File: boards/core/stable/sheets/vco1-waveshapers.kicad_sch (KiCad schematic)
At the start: 41 parts, among them U210 TL072, U211 TL072, U6 TL072

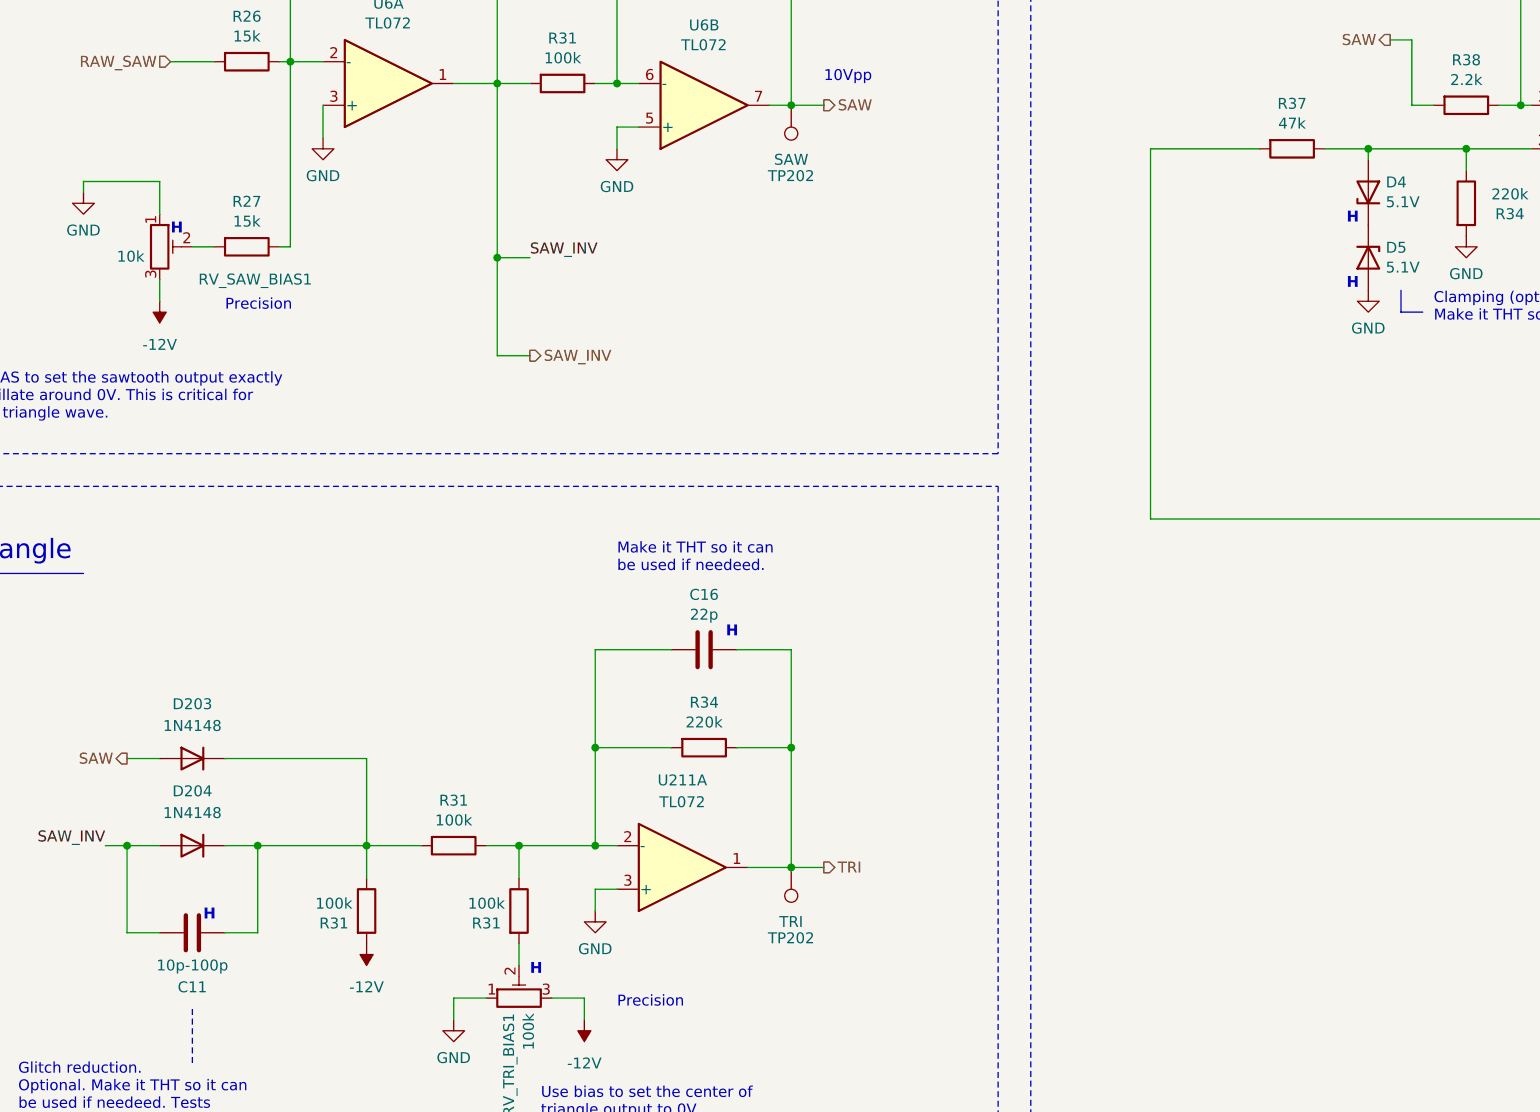
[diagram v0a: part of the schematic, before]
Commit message: Updated and checked Core board BOM
ref https://github.com/shmoergh/hog/issues/19
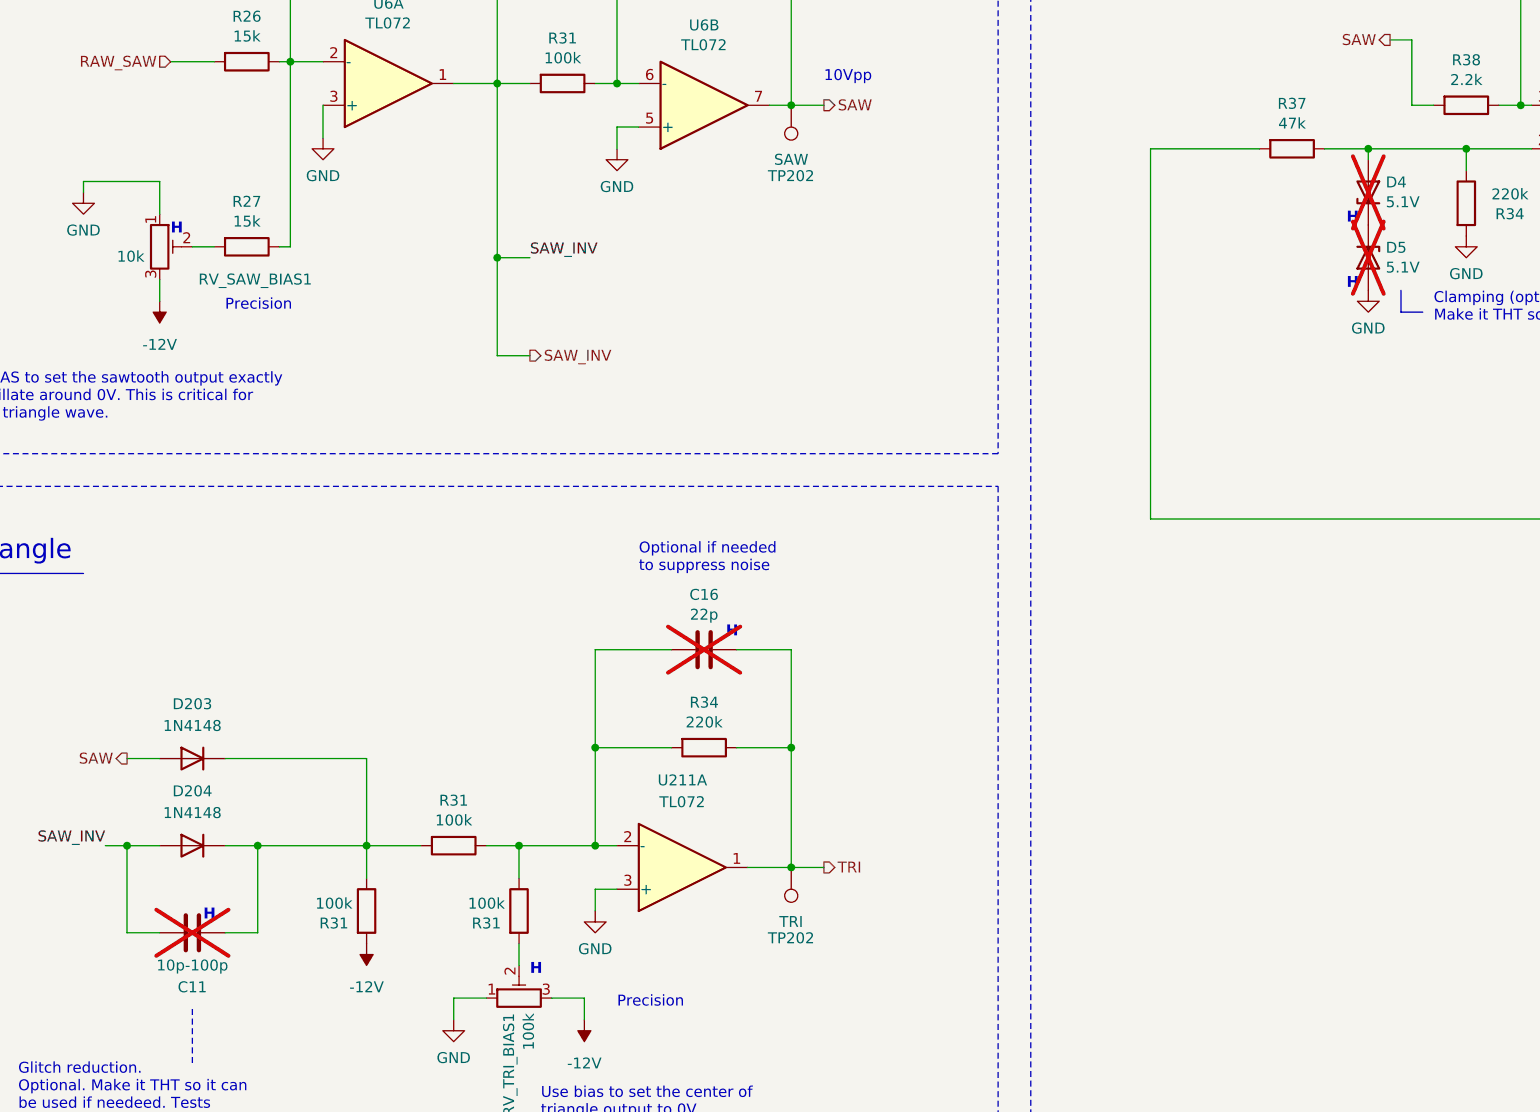
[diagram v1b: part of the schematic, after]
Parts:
- C11, C16, D4, D5: now not fitted
- C19, C203, D203, D204, R26, R27, R28, R31, R34, R37, R38, R41, R43, U210, U211, U6: Vendor (none) -> JLCPCB
- RV_SAW_BIAS1: Part No. (none) -> 652-3006P-1-103-LF; Part URL (none) -> https://mou.sr/41xh2vW; Vendor (none) -> Mouser; now in the parts list
- RV_TRI_BIAS1: Part No. (none) -> 652-3006P-1-104-LF; Part URL (none) -> https://mou.sr/4ff5W1E; Vendor (none) -> Mouser; now in the parts list
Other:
- note added: "Optional if needed to suppress noise"
- note removed: "Make it THT so it can be used if needeed."
